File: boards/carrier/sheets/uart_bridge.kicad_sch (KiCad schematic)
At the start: 7 parts, among them J1 TYPE-C-31-M-12, U1 CP2102N-A02-GQFN24R

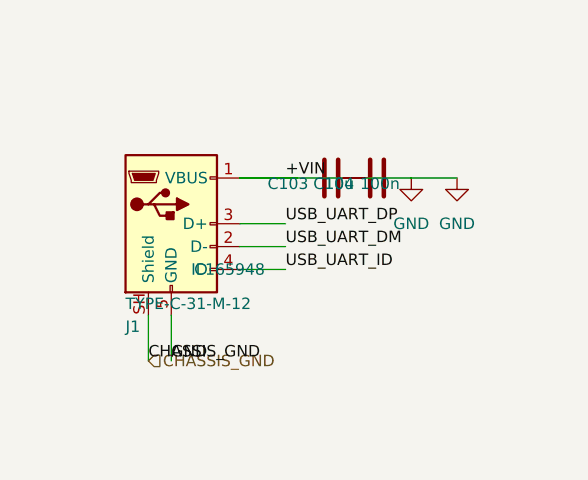
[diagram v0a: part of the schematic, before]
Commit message: Stage 5.5: rotation-derived pin sides + per-edge slot pitch (cluster fix)
Applies the in-flight cluster-fix agent's work (session limit cut its
own commit short). Two architectural changes that close the
sub-sheet wire_dangling / net-merging class of errors:

1) Rotation-derived page-side detection
   (core/layout/geometry.py + core/layout/cluster.py)

   Previously cluster.pin_side() compared abs(pin.x) vs abs(pin.y) on
   the symbol-relative coordinate to guess which body edge a pin
   emerges from. This mis-classified pins on ICs whose pin columns
   span a larger y-range than the body width — FUSB302's seven
   left-column pins (±7.62 mm in y) on a 20 mm-wide body wrap to
   "top/bottom" with the axis-dominance rule, but they're actually
   left-edge pins. The cluster then places passives on the wrong
   side and the resulting wires collide into other nets.

   The new page_side_from_pin() helper derives the page-side from the
   pin's intrinsic KiCad rotation (0 = LEFT edge, 90 = BOTTOM, 180 =
   RIGHT, 270 = TOP) combined with the placed symbol's rotation. This
   is the canonical KiCad convention and doesn't depend on body
   proportions.

   PinGeometry / PinGeometryAbs gain pin_rotation + symbol_rotation
   fields; SymbolGeometryCache reads pin.rotation from the cached
   SymbolDefinition (kicad-sch-api's list_pins() flattens it away).
   pin_side() takes optional pin_rotation/symbol_rotation; falls back
   to the legacy heuristic when not supplied.

2) Per-edge slot pitch
   (core/layout/_constants.py + core/layout/cluster.py)

   LEFT/RIGHT-edge passive swarms fan OUTWARD along the perpendicular
   axis: each slot is one passive body + one power-symbol stub further
   out. The pitch must clear 2 × PASSIVE_PIN_HALF (7.62 mm) +
   POWER_SYMBOL_OFFSET (5.08 mm), so HORIZONTAL_SWARM_PITCH_MM is now
   15.24 mm — was previously the same 5.08 mm used for TOP/BOTTOM, so
   adjacent slots' endpoints collapsed onto one another and KiCad
   merged the entire stack 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
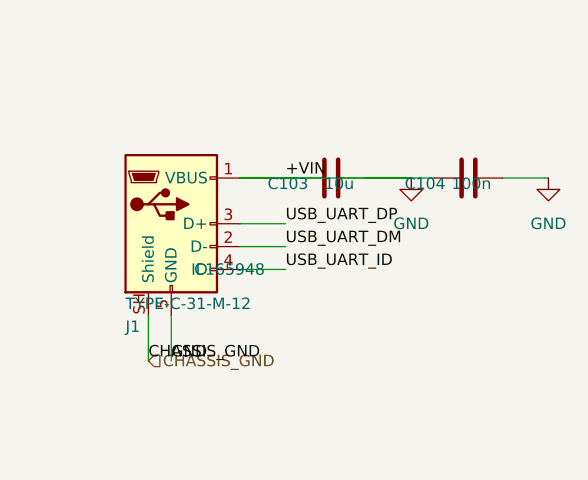
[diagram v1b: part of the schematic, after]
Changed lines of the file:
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@@
 		(instances
 			(project "USB-UART Bridge (CP2102N → Zynq PS UART0)"
-				(path "/a6266e3e-f106-445c-9ad2-624e9eecc0de"
+				(path "/77122c87-1a10-4bfa-83db-8af671214bb9"
 					(reference "U1")
 					(unit 1)
@@
 		(instances
 			(project "USB-UART Bridge (CP2102N → Zynq PS UART0)"
-				(path "/a6266e3e-f106-445c-9ad2-624e9eecc0de"
+				(path "/77122c87-1a10-4bfa-83db-8af671214bb9"
 					(reference "C100")
 					(unit 1)
@@
 		(instances
 			(project "USB-UART Bridge (CP2102N → Zynq PS UART0)"
-				(path "/a6266e3e-f106-445c-9ad2-624e9eecc0de"
+				(path "/77122c87-1a10-4bfa-83db-8af671214bb9"
 					(reference "#PWR100")
 					(unit 1)
@@
 		(instances
 			(project "USB-UART Bridge (CP2102N → Zynq PS UART0)"
-				(path "/a6266e3e-f106-445c-9ad2-624e9eecc0de"
+				(path "/77122c87-1a10-4bfa-83db-8af671214bb9"
 					(reference "C101")
 					(unit 1)
@@
 		(instances
 			(project "USB-UART Bridge (CP2102N → Zynq PS UART0)"
-				(path "/a6266e3e-f106-445c-9ad2-624e9eecc0de"
+				(path "/77122c87-1a10-4bfa-83db-8af671214bb9"
 					(reference "#PWR101")
 					(unit 1)
@@
 		(instances
 			(project "USB-UART Bridge (CP2102N → Zynq PS UART0)"
-				(path "/a6266e3e-f106-445c-9ad2-624e9eecc0de"
+				(path "/77122c87-1a10-4bfa-83db-8af671214bb9"
 					(reference "C102")
 					(unit 1)
@@
 		(instances
 			(project "USB-UART Bridge (CP2102N → Zynq PS UART0)"
-				(path "/a6266e3e-f106-445c-9ad2-624e9eecc0de"
+				(path "/77122c87-1a10-4bfa-83db-8af671214bb9"
 					(reference "#PWR102")
 					(unit 1)
@@
 		(instances
 			(project "USB-UART Bridge (CP2102N → Zynq PS UART0)"
-				(path "/a6266e3e-f106-445c-9ad2-624e9eecc0de"
+				(path "/77122c87-1a10-4bfa-83db-8af671214bb9"
 					(reference "#PWR103")
 					(unit 1)
@@
 		(instances
 			(project "USB-UART Bridge (CP2102N → Zynq PS UART0)"
-				(path "/a6266e3e-f106-445c-9ad2-624e9eecc0de"
+				(path "/77122c87-1a10-4bfa-83db-8af671214bb9"
 					(reference "#PWR104")
 					(unit 1)
@@
 		(instances
 			(project "USB-UART Bridge (CP2102N → Zynq PS UART0)"
-				(path "/a6266e3e-f106-445c-9ad2-624e9eecc0de"
+				(path "/77122c87-1a10-4bfa-83db-8af671214bb9"
 					(reference "J1")
 					(unit 1)
@@
 		(instances
 			(project "USB-UART Bridge (CP2102N → Zynq PS UART0)"
-				(path "/a6266e3e-f106-445c-9ad2-624e9eecc0de"
+				(path "/77122c87-1a10-4bfa-83db-8af671214bb9"
 					(reference "C103")
 					(unit 1)
@@
 		(instances
 			(project "USB-UART Bridge (CP2102N → Zynq PS UART0)"
-				(path "/a6266e3e-f106-445c-9ad2-624e9eecc0de"
+				(path "/77122c87-1a10-4bfa-83db-8af671214bb9"
 					(reference "#PWR105")
 					(unit 1)
@@
 	(symbol
 		(lib_id "Device:C")
-		(at 259.08 30.48 90)
+		(at 269.24 30.48 90)
 		(unit 1)
 		(exclude_from_sim no)
@@
 		(fields_autoplaced no)
 		(property "Reference" "C104"
-			(at 256.54 31.115 90)
+			(at 266.7 31.115 90)
 			(effects
 				(font
@@
 		)
 		(property "Value" "100n"
-			(at 261.62 31.115 90)
+			(at 271.78 31.115 90)
 			(effects
 				(font
@@
 		)
 		(property "Footprint" "Capacitor_SMD:C_0402_1005Metric"
-			(at 260.0452 26.67 0.0000)
+			(at 270.2052 26.67 0.0000)
 			(effects
 				(font
@@
 		(instances
 			(project "USB-UART Bridge (CP2102N → Zynq PS UART0)"
-				(path "/a6266e3e-f106-445c-9ad2-624e9eecc0de"
+				(path "/77122c87-1a10-4bfa-83db-8af671214bb9"
 					(reference "C104")
 					(unit 1)
@@
 	(symbol
 		(lib_id "power:GND")
-		(at 267.97 30.48 0)
+		(at 278.13 30.48 0)
 		(unit 1)
 		(exclude_from_sim no)
@@
 		(fields_autoplaced no)
 		(property "Reference" "#PWR106"
-			(at 267.97 24.13 0.0000)
+			(at 278.13 24.13 0.0000)
 			(effects
 				(font
@@
 		)
 		(property "Value" "GND"
-			(at 267.97 35.56 0)
+			(at 278.13 35.56 0)
 			(effects
 				(font
@@
 		)
 		(property "Footprint" ""
-			(at 267.97 30.48 0.0000)
-			(effects
-				(font
-					(size 1.27 1.27)
-				)
-				(hide yes)
-			)
-		)
-		(pin "1"
-		)
-		(instances
-			(project "USB-UART Bridge (CP2102N → Zynq PS UART0)"
-				(path "/a6266e3e-f106-445c-9ad2-624e9eecc0de"
+			(at 278.13 30.48 0.0000)
+			(effects
+				(font
+					(size 1.27 1.27)
+				)
+				(hide yes)
+			)
+		)
+		(pin "1"
+		)
+		(instances
+			(project "USB-UART Bridge (CP2102N → Zynq PS UART0)"
+				(path "/77122c87-1a10-4bfa-83db-8af671214bb9"
 					(reference "#PWR106")
 					(unit 1)
@@
 		(instances
 			(project "USB-UART Bridge (CP2102N → Zynq PS UART0)"
-				(path "/a6266e3e-f106-445c-9ad2-624e9eecc0de"
+				(path "/77122c87-1a10-4bfa-83db-8af671214bb9"
 					(reference "#PWR107")
 					(unit 1)
@@
 	(wire
 		(pts
-			(xy 243.84 30.48) (xy 255.27 30.48)
-		)
-		(stroke
-			(width 0)
-			(type default)
-		)
-	)
-	(wire
-		(pts
-			(xy 262.89 30.48) (xy 267.97 30.48)
-		)
-		(stroke
+			(xy 243.84 30.48) (xy 265.43 30.48)
+		)
+		(stroke
+			(width 0)
+			(type default)
+		)
+	)
+	(wire
+		(pts
+			(xy 273.05 30.48) (xy 278.13 30.48)
+		)
+		(stroke
